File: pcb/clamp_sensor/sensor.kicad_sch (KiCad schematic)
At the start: 7 parts, among them J1 Conn_01x08

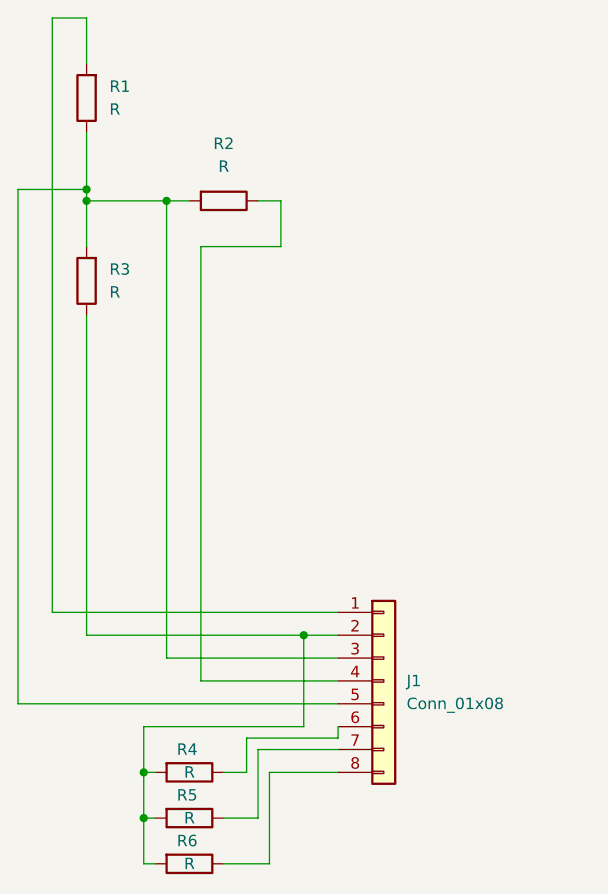
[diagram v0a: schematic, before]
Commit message: PCB: Clamp sensor update
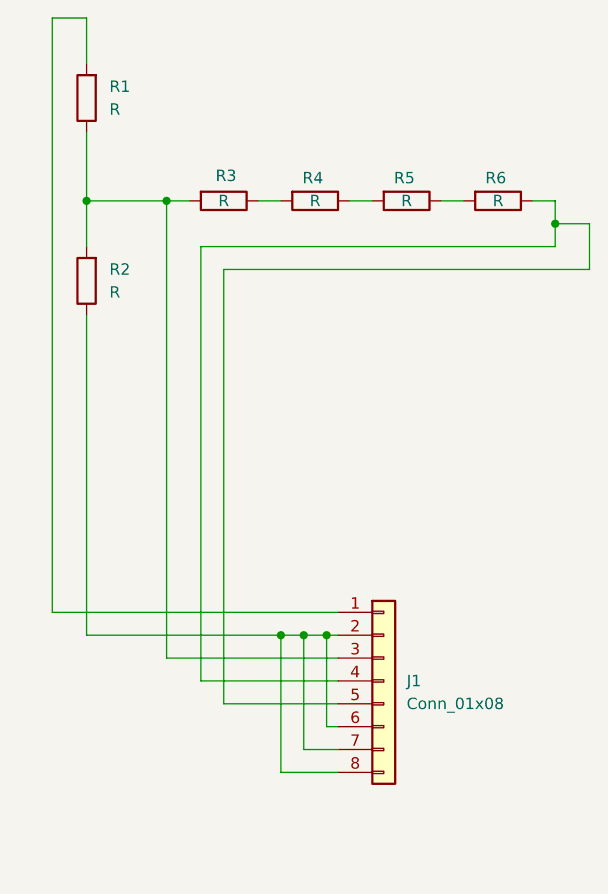
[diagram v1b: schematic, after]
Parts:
- renumbered R3 to R2, R2 to R3
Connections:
- net at R6.1: now also J1.4 (Pin_4), J1.5 (Pin_5); no longer J1.8 (Pin_8)
- net at J1.3 (Pin_3), R1.1, R2.2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: no longer J1.5 (Pin_5)
- net at R3.1: now also R4.2; no longer J1.4 (Pin_4)
- net at J1.6 (Pin_6): now also J1.2 (Pin_2), J1.7 (Pin_7), J1.8 (Pin_8), R2.1; no longer R4.1
- net at R5.1: now also R6.2; no longer J1.7 (Pin_7)
- new net: R4.1, R5.2
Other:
- moved on the sheet: R4, R5, R6
